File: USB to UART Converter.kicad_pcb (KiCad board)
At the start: 2 copper layers, 19 parts, among them J1 USB_C_Receptacle_USB2.0_16P, J2 Conn_01x05_Pin, U1 CP2102N-Axx-xQFN28

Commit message: Placed Footprints In PCB Editor
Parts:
- moved J2 35.3 mm to (168.8, 97.6)
- moved D3 27.1 mm to (150.5, 106.2), turned to 90 degrees
- moved D1 26.2 mm to (162.7, 100.2)
- moved D2 26.1 mm to (162.7, 101.5)
- moved D4 24.0 mm to (153.0, 106.2), turned to 90 degrees
- moved R4 22.9 mm to (164.9, 104.0)
- moved D5 21.9 mm to (148.0, 106.1), turned to 90 degrees
- moved R5 21.9 mm to (162.7, 104.0)
- moved R6 20.6 mm to (164.9, 100.2)
- moved J1 20.4 mm to (140.8, 103.2), turned to -90 degrees
- moved R7 20.4 mm to (164.9, 101.5)
- moved R3 18.5 mm to (155.4, 107.2)
- moved C1 17.7 mm to (152.4, 103.2)
- moved C2 15.8 mm to (155.5, 98.6), turned to 90 degrees
- moved C3 14.1 mm to (153.0, 101.1), turned to 90 degrees
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
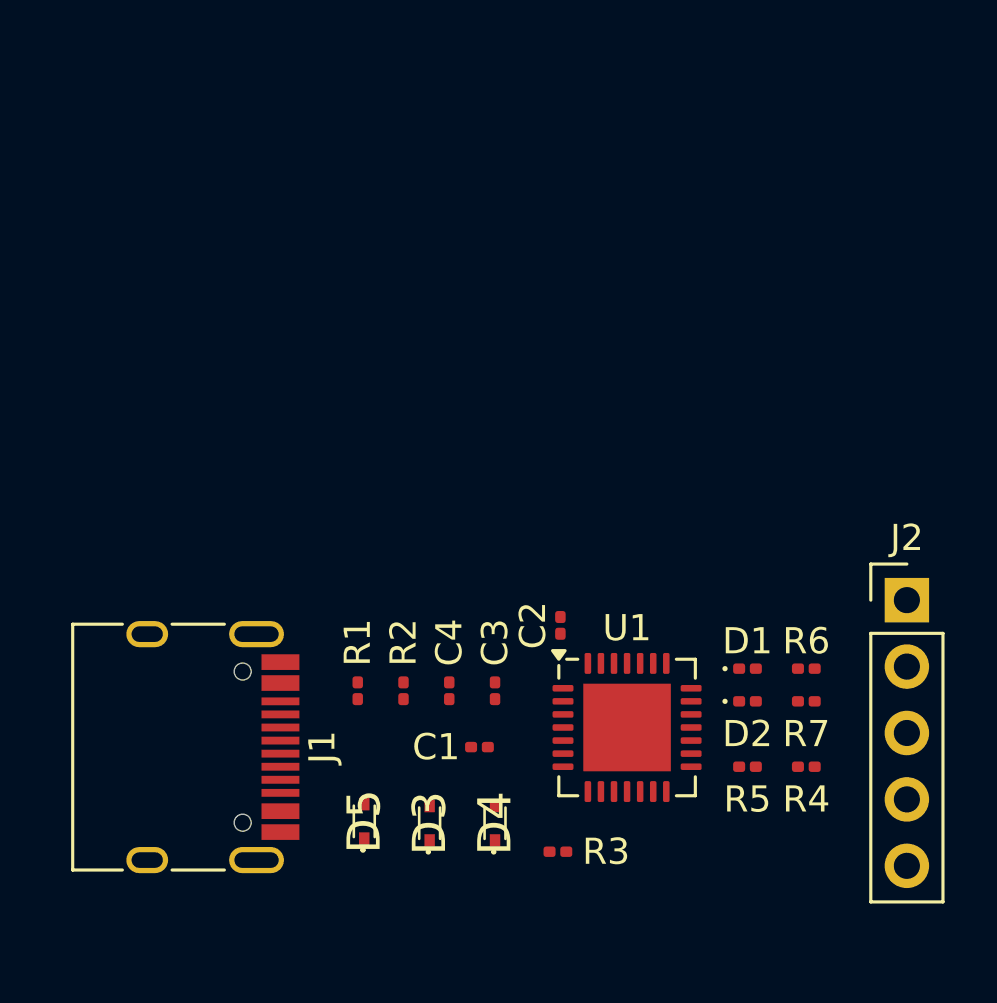
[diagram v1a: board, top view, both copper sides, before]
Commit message: Added Tracks to Footprints
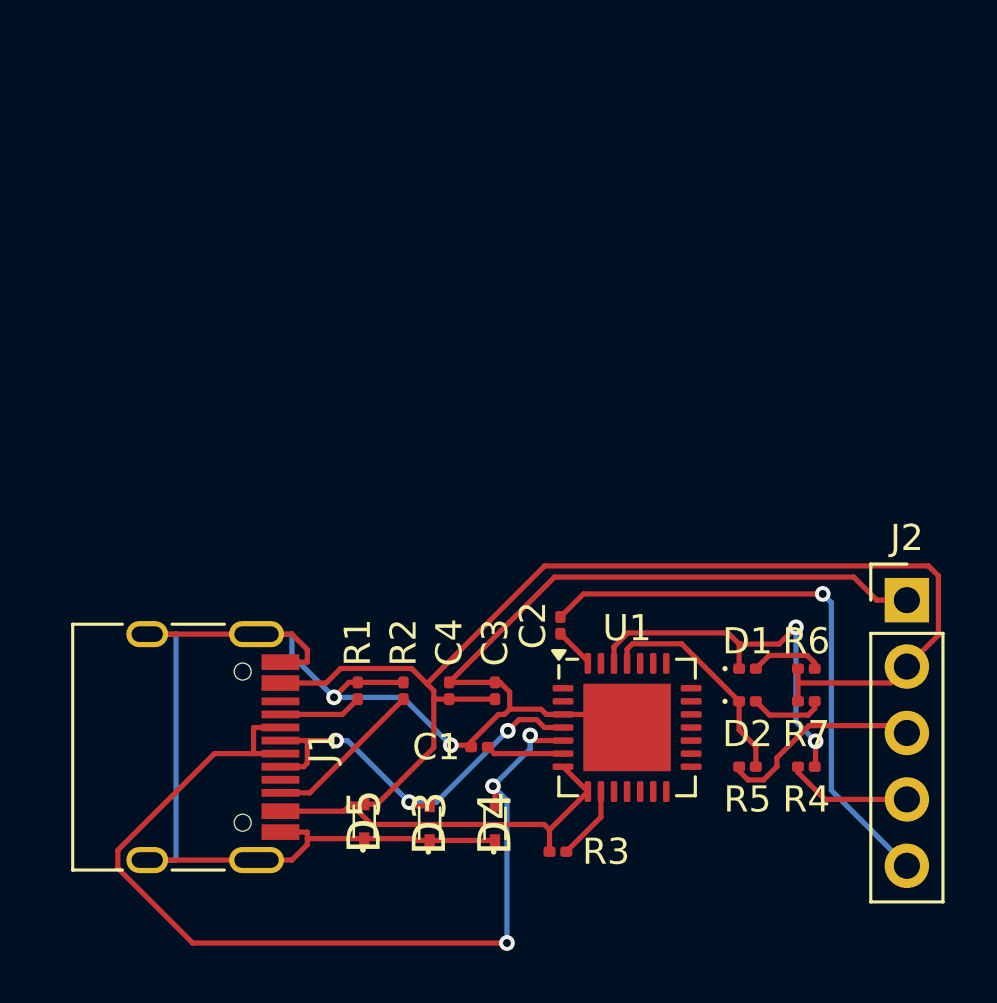
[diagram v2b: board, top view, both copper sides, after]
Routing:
- net GND: track 0.00 -> 76.8 mm, vias 0 -> 2
- net /VBUS: track 0.00 -> 61.3 mm
- net /D-: track 0.00 -> 37.4 mm, vias 0 -> 3
- net /RST: track 0.00 -> 22.1 mm, vias 0 -> 1
- net /D+: track 0.00 -> 16.0 mm, vias 0 -> 3
- net Net-(D1-K): track 0.00 -> 14.9 mm, vias 0 -> 2
- net Net-(D2-K): track 0.00 -> 8.59 mm
- net /RX: track 0.00 -> 7.89 mm
- net Net-(J1-CC2): track 0.00 -> 6.19 mm
- net /TX: track 0.00 -> 4.81 mm
- net Net-(J1-CC1): track 0.00 -> 3.20 mm
- net Net-(U1-VDD): track 0.00 -> 2.98 mm
- net Net-(U1-~{RST}): track 0.00 -> 2.85 mm
- net Net-(D2-A): track 0.00 -> 2.85 mm
- net Net-(D1-A): track 0.00 -> 2.80 mm
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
